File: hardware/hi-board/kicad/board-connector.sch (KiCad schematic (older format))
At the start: 1 part, among them J1 Conn_02x25_Counter_Clockwise

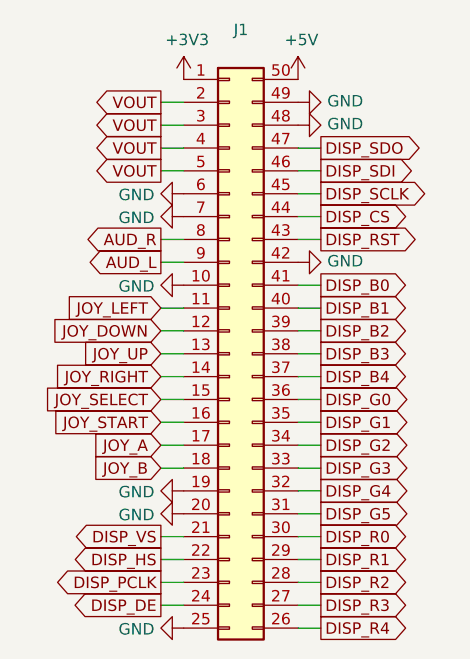
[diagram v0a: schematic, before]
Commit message: Place connector components
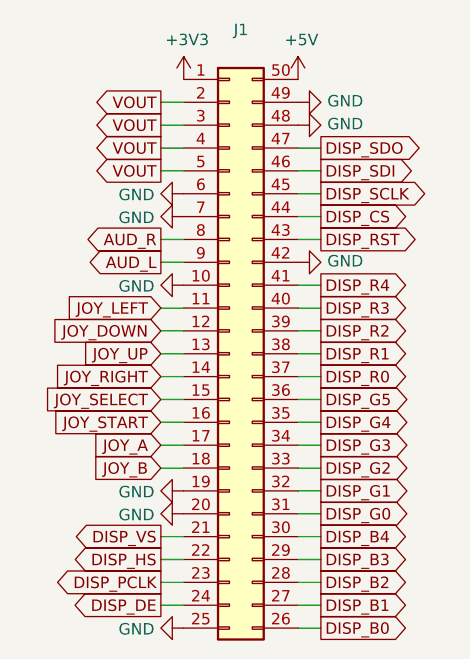
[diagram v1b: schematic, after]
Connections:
- net DISP_B0: now also J1.26 (Pin_26); no longer J1.41 (Pin_41)
- net DISP_B1: now also J1.27 (Pin_27); no longer J1.40 (Pin_40)
- net DISP_B2: now also J1.28 (Pin_28); no longer J1.39 (Pin_39)
- net DISP_B3: now also J1.29 (Pin_29); no longer J1.38 (Pin_38)
- net DISP_B4: now also J1.30 (Pin_30); no longer J1.37 (Pin_37)
- net DISP_G0: now also J1.31 (Pin_31); no longer J1.36 (Pin_36)
- net DISP_G1: now also J1.32 (Pin_32); no longer J1.35 (Pin_35)
- net DISP_G2: now also J1.33 (Pin_33); no longer J1.34 (Pin_34)
- net DISP_G3: now also J1.34 (Pin_34); no longer J1.33 (Pin_33)
- net DISP_G4: now also J1.35 (Pin_35); no longer J1.32 (Pin_32)
- net DISP_G5: now also J1.36 (Pin_36); no longer J1.31 (Pin_31)
- net DISP_R0: now also J1.37 (Pin_37); no longer J1.30 (Pin_30)
- net DISP_R1: now also J1.38 (Pin_38); no longer J1.29 (Pin_29)
- net DISP_R2: now also J1.39 (Pin_39); no longer J1.28 (Pin_28)
- net DISP_R3: now also J1.40 (Pin_40); no longer J1.27 (Pin_27)
- net DISP_R4: now also J1.41 (Pin_41); no longer J1.26 (Pin_26)
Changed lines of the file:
@@
 Text GLabel 6050 3150 2    50   Output ~ 0
 DISP_RST
+Text GLabel 6050 4850 2    50   Output ~ 0
+DISP_B0
+Text GLabel 6050 4750 2    50   Output ~ 0
+DISP_B1
+Text GLabel 6050 4650 2    50   Output ~ 0
+DISP_B2
+Text GLabel 6050 4550 2    50   Output ~ 0
+DISP_B3
+Text GLabel 6050 4450 2    50   Output ~ 0
+DISP_B4
+Text GLabel 6050 4350 2    50   Output ~ 0
+DISP_G0
+Text GLabel 6050 4250 2    50   Output ~ 0
+DISP_G1
+Text GLabel 6050 4150 2    50   Output ~ 0
+DISP_G2
+Text GLabel 6050 4050 2    50   Output ~ 0
+DISP_G3
+Text GLabel 6050 3950 2    50   Output ~ 0
+DISP_G4
+Text GLabel 6050 3850 2    50   Output ~ 0
+DISP_G5
+Text GLabel 6050 3750 2    50   Output ~ 0
+DISP_R0
+Text GLabel 6050 3650 2    50   Output ~ 0
+DISP_R1
+Text GLabel 6050 3550 2    50   Output ~ 0
+DISP_R2
+Text GLabel 6050 3450 2    50   Output ~ 0
+DISP_R3
 Text GLabel 6050 3350 2    50   Output ~ 0
-DISP_B0
-Text GLabel 6050 3450 2    50   Output ~ 0
-DISP_B1
-Text GLabel 6050 3550 2    50   Output ~ 0
-DISP_B2
-Text GLabel 6050 3650 2    50   Output ~ 0
-DISP_B3
-Text GLabel 6050 3750 2    50   Output ~ 0
-DISP_B4
-Text GLabel 6050 3850 2    50   Output ~ 0
-DISP_G0
-Text GLabel 6050 3950 2    50   Output ~ 0
-DISP_G1
-Text GLabel 6050 4050 2    50   Output ~ 0
-DISP_G2
-Text GLabel 6050 4150 2    50   Output ~ 0
-DISP_G3
-Text GLabel 6050 4250 2    50   Output ~ 0
-DISP_G4
-Text GLabel 6050 4350 2    50   Output ~ 0
-DISP_G5
-Text GLabel 6050 4450 2    50   Output ~ 0
-DISP_R0
-Text GLabel 6050 4550 2    50   Output ~ 0
-DISP_R1
-Text GLabel 6050 4650 2    50   Output ~ 0
-DISP_R2
-Text GLabel 6050 4750 2    50   Output ~ 0
-DISP_R3
-Text GLabel 6050 4850 2    50   Output ~ 0
 DISP_R4
 $EndSCHEMATC
